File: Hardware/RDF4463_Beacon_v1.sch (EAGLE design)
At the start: 12 parts, among them M1 DORJI_DRF4463F, U1 PIC18F24K22

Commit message: Guncelleme
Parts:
- added C17: 100n, AVX_By_element14_Batch_1:0805YD106MAT2A
- added C18: 100p, AVX_By_element14_Batch_1:0805YD106MAT2A
- added C4: 10UF, AVX_By_element14_Batch_1:0805YD106MAT2A
- added C5: 0.1UF, AVX_By_element14_Batch_1:0805ZC104MAT2A
- added IC1: LD117AS33TR, v-reg:LD117AS33TR
- added R4, R5: (no value), rcl:R-EU_R0805
- added SV1: (no value), con-lsta:FE05-1
- added VIN: (no value), con-molex:KK-156-2
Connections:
- new net +3V3: C17.C2, C18.C2, C4.C2, IC1.OUT, M1.5
- new net ADC: R4.1, R5.2, U1.RA0/AN0/C12IN0-
- new net MCLR: SV1.1, U1.~MCLR/VPP/RE3
- new net N$2: ANT1.1, M1.13
- new net N$8: LED2.C, R2.2
- new net RB6: SV1.4
- new net VIN: C5.C2, IC1.IN, R4.2, VIN-1.S
- net GND: now also C17.C1, C18.C1, C4.C1, C5.C1, IC1.ADJ, M1.14, R5.1, SV1.3, VIN-2.S
- net N$9: now also LED1.C
- net RB7: now also SV1.5
- net SDI: now also U1.RB5/KBI1/PGM; no longer U1.RB4/KBI0/AN11/P1D
- net SDO: now also U1.RB4/KBI0/AN11/P1D; no longer U1.RB5/KBI1/PGM
- net VCC: now also SV1.2; no longer M1.5
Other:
- moved on the sheet: ANT1, LED2, R3

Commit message: PCB yi cizmeye basladim
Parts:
- ANT1: value (none) -> ANT
- C1, C2: value (none) -> 15p
- C3: value (none) -> 10n
- LED1: value (none) -> Y
- LED2: value (none) -> K
- Q1: value (none) -> 20M
- R1, R4: value (none) -> 10K
- R2, R3, R5: value (none) -> 1K
- SV1: value (none) -> ICD
- VIN: value (none) -> INPUT
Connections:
- removed net GPIO0: M1.3
- removed net GPIO1: M1.4
- removed net N$10: R2.1, R3.1
- removed net N$5: R1.1
- net GND: now also R2.1, R3.1
- net MCLR: now also R1.1
- net RB6: now also U1.RB6/KBI2/PGC
- net SCLK: now also U1.RB3/AN9/C12IN2-/CCP2
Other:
- moved on the sheet: R4, U1

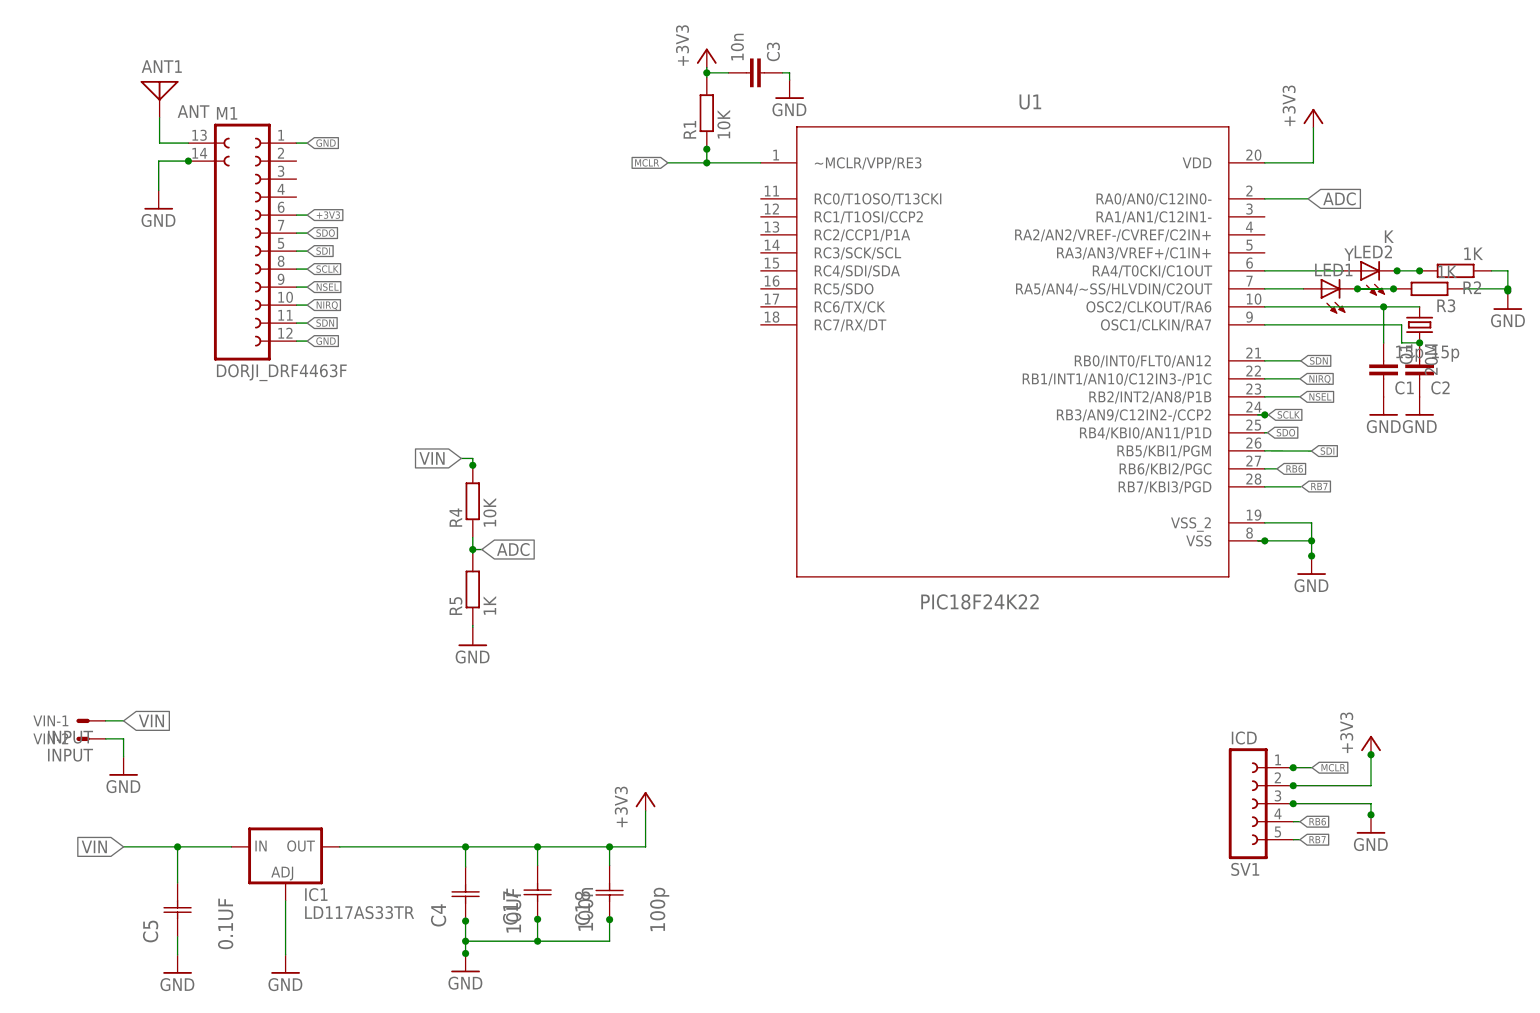
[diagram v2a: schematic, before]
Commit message: once -SS kilif a gore cizmistim
Bu versiyonda degistiriyorum.. -SO klifli PIC e gorre yaptim

bu kartin buyuk bir bolumunu ICD konnektoru ve DATA RXTX konnektoru tutuyor
simdilik bunu bir EVALUATION karti gibi kullanacagim

Daha sonra yapacaklarim sunlardir :
------------------------------------

1) PIC'i APRS kullanimi icin 16F628 gibi kucuk bir PIC ile degistirmek
2) secilecek PIC'in 3.3V ile calisan versiyonunu tercih etmek
3) MTK GPS i de ekleyip ondan gelen datalari okumak
4) MTK GPS i iceren bir kart cizmek
5) vesaire vesaire
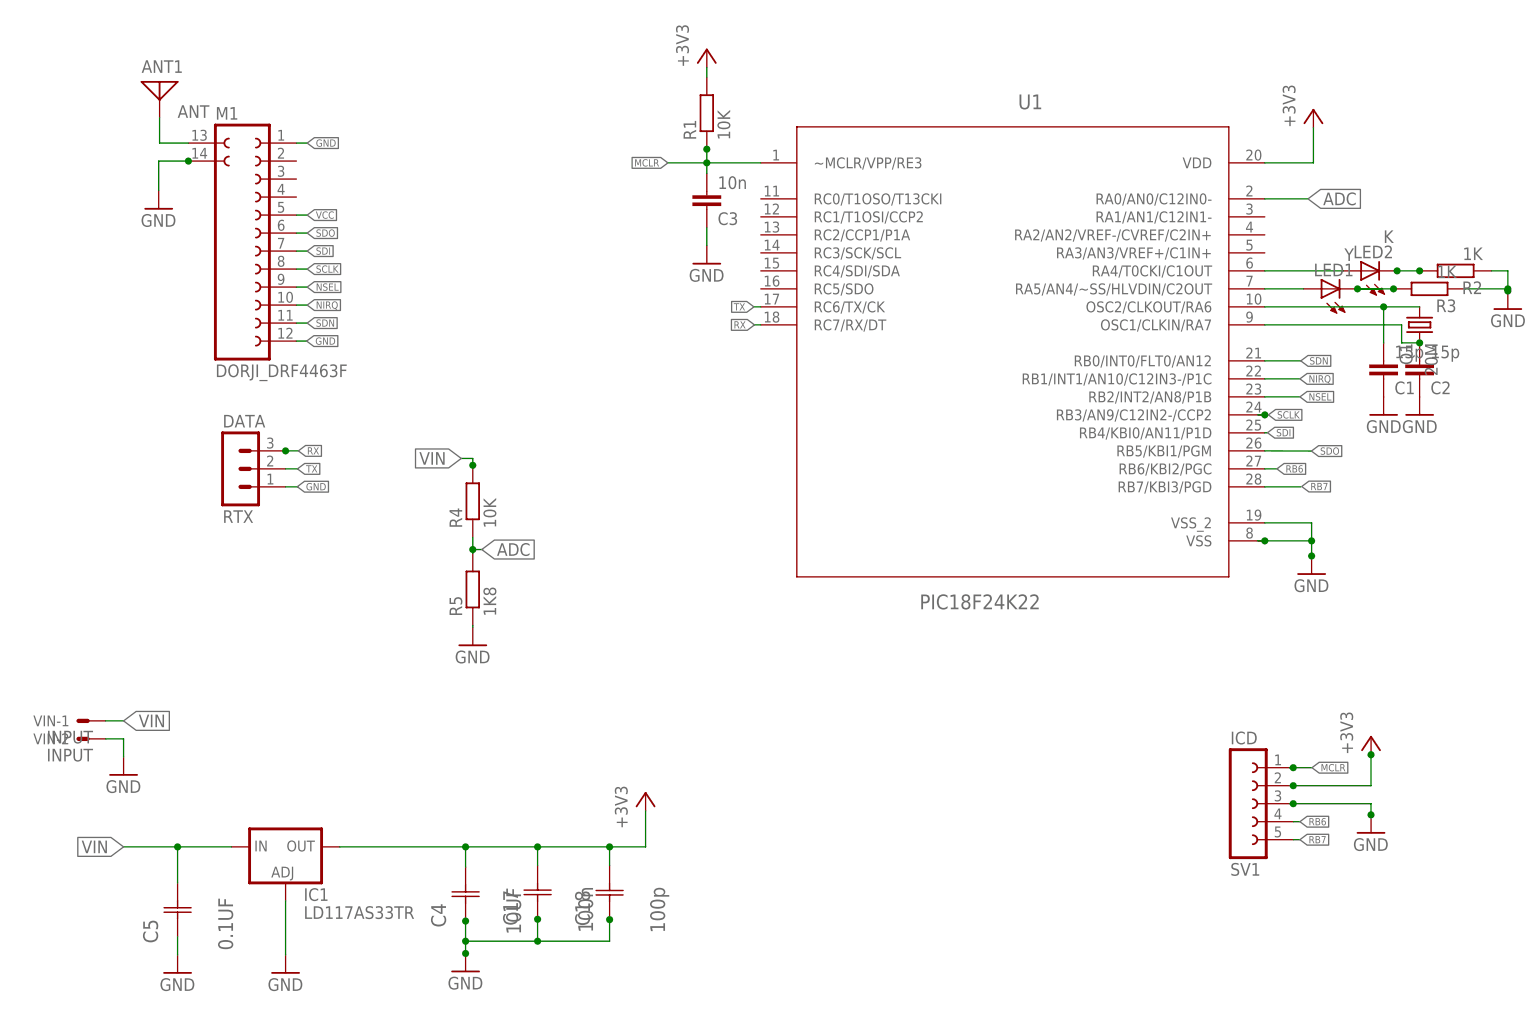
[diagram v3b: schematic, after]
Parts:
- added DATA: RTX, con-lstb:MA03-1
- LED1, LED2: device led:LEDSML0603 -> led:LEDSML0805
- R5: value 1K -> 1K8
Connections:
- removed net +3V3: C17.C2, C18.C2, C4.C2, IC1.OUT, M1.5
- new net RX: DATA.3, U1.RC7/RX/DT
- new net TX: DATA.2, U1.RC6/TX/CK
- net GND: now also DATA.1
- net MCLR: now also C3.2
- net SDI: now also U1.RB4/KBI0/AN11/P1D; no longer U1.RB5/KBI1/PGM
- net SDO: now also U1.RB5/KBI1/PGM; no longer U1.RB4/KBI0/AN11/P1D
- net VCC: now also C17.C2, C18.C2, C4.C2, IC1.OUT, M1.5; no longer C3.2
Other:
- moved on the sheet: C3
